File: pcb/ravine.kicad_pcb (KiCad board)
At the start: 2 copper layers, 102 x 101.7 mm, 39 parts

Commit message: okay last save before converting to normie matrix
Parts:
- removed PLACEHOLDER: , placeholder
- added ?: , footprints:xiao-pogo-rev, F.Cu at (155.5, 163.1)
- added CR1: , footprints:bs-2032-8_rev, F.Cu at (185.5, 189.5)
- added D17: , footprints:diode_rev, F.Cu at (198.5, 165.8)
- added D18: , footprints:diode_rev, F.Cu at (204.6, 147.8)
- added D19: , footprints:diode_rev, F.Cu at (210.7, 129.8)
- added D20: , footprints:diode_rev, F.Cu at (220.5, 160.2)
- added D21: , footprints:diode_rev, F.Cu at (226.6, 142.2)
- added D22: , footprints:diode_rev, F.Cu at (231.4, 178.2)
- added D23: , footprints:diode_rev, F.Cu at (160.2, 182.9)
- added D24: , footprints:diode_rev, F.Cu at (160.4, 121.8)
- added D25: , footprints:diode_rev, F.Cu at (156.4, 140.4)
- added D26: , footprints:diode_rev, F.Cu at (175.2, 170.0)
- added XX1: , footprints:slider-mss22d18_rev, F.Cu at (209.0, 186.5)
- B1: footprint E73:SW_TACT_ALPS_SKQGABE010 -> footprints:alps-skqg_rev
- D1, D10, D11, D12, D13, D14, D15, D16, D2, D3, D4, D5, D6, D7, D8, D9: footprint diode-rev -> footprints:diode_rev
- SW1, SW10, SW11, SW12, SW13, SW14, SW15, SW16, SW2, SW3, SW4, SW5, SW6, SW7, SW8, SW9: footprint hs-mx-choc-rev -> footprints:hs-mx-choc_rev
- moved D9 79.9 mm to (157.1, 149.0), turned to 119.333 degrees
- moved D8 71.4 mm to (154.4, 144.1), turned to 119.333 degrees
- moved D7 66.8 mm to (154.3, 148.3), turned to 119.333 degrees
- moved D6 60.5 mm to (151.6, 143.3), turned to 119.333 degrees
- moved D16 58.8 mm to (195.1, 116.5), turned to -18.666 degrees
- moved D3 55.2 mm to (148.7, 146.7), turned to 119.333 degrees
- moved D4 54.7 mm to (148.8, 142.6), turned to 119.333 degrees
- moved D5 52.9 mm to (151.5, 147.5), turned to 119.333 degrees
- moved D2 43.5 mm to (146.0, 141.8), turned to 119.333 degrees
- moved D14 39.9 mm to (183.0, 152.6), turned to -18.6667 degrees
- moved JST1 39.4 mm to (206.0, 194.8), turned to 90 degrees
- moved D1 37.4 mm to (145.9, 145.9), turned to 119.333 degrees
- moved D15 33.2 mm to (189.1, 134.6), turned to -18.6667 degrees
- moved D10 23.4 mm to (157.2, 144.9), turned to 119.333 degrees
- moved D11 10.0 mm to (163.2, 151.7), turned to -15.6667 degrees
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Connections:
- D1 pad 1: middle_bottom -> D6
- D1 pad 2: (no net) -> P6
- D10 pad 1: pinky_top -> D10
- D10 pad 2: P0 -> intr
- D11 pad 2: (no net) -> D9
- D12 pad 2: (no net) -> D9
- D13 pad 2: (no net) -> D9
- D14 pad 1: default_default -> middle_bottom
- D14 pad 2: P3 -> D8
- D15 pad 1: pinky_home -> middle_home
- D15 pad 2: P0 -> D8
- D16 pad 1: default_default -> middle_top
- D16 pad 2: P2 -> D8
- D2 pad 1: middle_home -> D6
- D2 pad 2: (no net) -> intr
- D3 pad 1: middle_top -> D7
- D3 pad 2: (no net) -> P7
- D4 pad 1: index_bottom -> D7
- D4 pad 2: P3 -> intr
- D5 pad 1: index_home -> D8
- D5 pad 2: P3 -> P8
- D6 pad 1: index_top -> D8
- D6 pad 2: P3 -> intr
- D7 pad 1: inner_home -> D9
- D7 pad 2: P4 -> P9
- D8 pad 1: inner_top -> D9
- D8 pad 2: P4 -> intr
- D9 pad 1: default_default -> D10
- D9 pad 2: P0 -> P10
- JST1 pad 1: battery -> jst_bat
- RE1 pad S1: default_default -> P7
- RE1 pad S2: P3 -> default_default
- SW1 pad 1: P1 -> P9
- SW10 pad 1: P1 -> P9
- SW11 pad 1: P0 -> P10
- SW12 pad 1: P1 -> P9
- SW13 pad 1: P0 -> P10
- SW14 pad 1: P3 -> P7
- SW15 pad 1: P3 -> P7
- SW15 pad 2: default_default -> thumb_default
- SW16 pad 1: P4 -> P6
- SW2 pad 1: P0 -> P6
- SW3 pad 1: P2 -> P8
- SW4 pad 1: P4 -> P6
- SW5 pad 1: P0 -> P10
- SW6 pad 1: P4 -> P6
- SW7 pad 1: P1 -> P9
- SW8 pad 1: P0 -> P10
- SW9 pad 1: P2 -> P8
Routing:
- net P10: track 0.00 -> 15.0 mm
- net intr: track 0.00 -> 11.6 mm
- net ring_top: track 0.00 -> 11.1 mm
- net pinky_top: track 0.00 -> 6.15 mm
- net trrs: track 0.00 -> 4.60 mm
- net VCC: track 0.00 -> 4.60 mm
- net D7: track 0.00 -> 4.12 mm
- net D10: track 0.00 -> 4.12 mm
- net D8: track 0.00 -> 4.12 mm
- net D6: track 0.00 -> 4.12 mm
- net D9: track 0.00 -> 4.12 mm
- net middle_top: track 0.00 -> 3.75 mm
- net inner_top: track 0.00 -> 3.75 mm
- net index_top: track 0.00 -> 3.75 mm
- net P6: track 0.00 -> 3.75 mm
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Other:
- board size 102 x 101.7 mm -> 102 x 101.9 mm

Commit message: ok fr this time before matrix
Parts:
- removed the ? at (155.5, 163.1)
- added ?: , xiao-ble, F.Cu at (155.5, 163.1)
- B1: footprint footprints:alps-skqg_rev -> E73:SW_TACT_ALPS_SKQGABE010
- CR1: footprint footprints:bs-2032-8_rev -> bs-2032-8_rev
- D1, D10, D11, D12, D13, D14, D15, D16, D17, D18, D19, D2, D20, D21, D22, D23, D24, D25, D26, D3, D4, D5, D6, D7, D8, D9: footprint footprints:diode_rev -> diode-rev
- SW1, SW10, SW11, SW12, SW13, SW14, SW15, SW16, SW2, SW3, SW4, SW5, SW6, SW7, SW8, SW9: footprint footprints:hs-mx-choc_rev -> hs-mx-choc-rev
- XX1: footprint footprints:slider-mss22d18_rev -> slider-mss22d18_rev
- moved PWR1 0.10 mm to (234.2, 121.9), turned to 45.3333 degrees
- turned D18 to -18.6667 degrees
- turned D15 to -18.6667 degrees
- turned D26 to -18.6667 degrees
- turned TRRS1 to -18.6667 degrees
- turned D4 to 119.333 degrees
- turned SW1 to 169.333 degrees
- turned D24 to 169.333 degrees
- turned D22 to -128.667 degrees
- turned D5 to 119.333 degrees
- turned D8 to 119.333 degrees
- turned D9 to 119.333 degrees
- turned D11 to -15.6667 degrees
- turned SW3 to -15.6667 degrees
- turned SW4 to -15.6667 degrees
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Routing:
- net P10: track 15.0 -> 0.00 mm
- net intr: track 11.6 -> 0.00 mm
- net ring_top: track 11.1 -> 0.00 mm
- net pinky_top: track 6.15 -> 0.00 mm
- net trrs: track 4.60 -> 0.00 mm
- net VCC: track 4.60 -> 0.00 mm
- net D7: track 4.12 -> 0.00 mm
- net D10: track 4.12 -> 0.00 mm
- net D8: track 4.12 -> 0.00 mm
- net D6: track 4.12 -> 0.00 mm
- net D9: track 4.12 -> 0.00 mm
- net middle_top: track 3.75 -> 0.00 mm
- net inner_top: track 3.75 -> 0.00 mm
- net index_top: track 3.75 -> 0.00 mm
- net P6: track 3.75 -> 0.00 mm
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
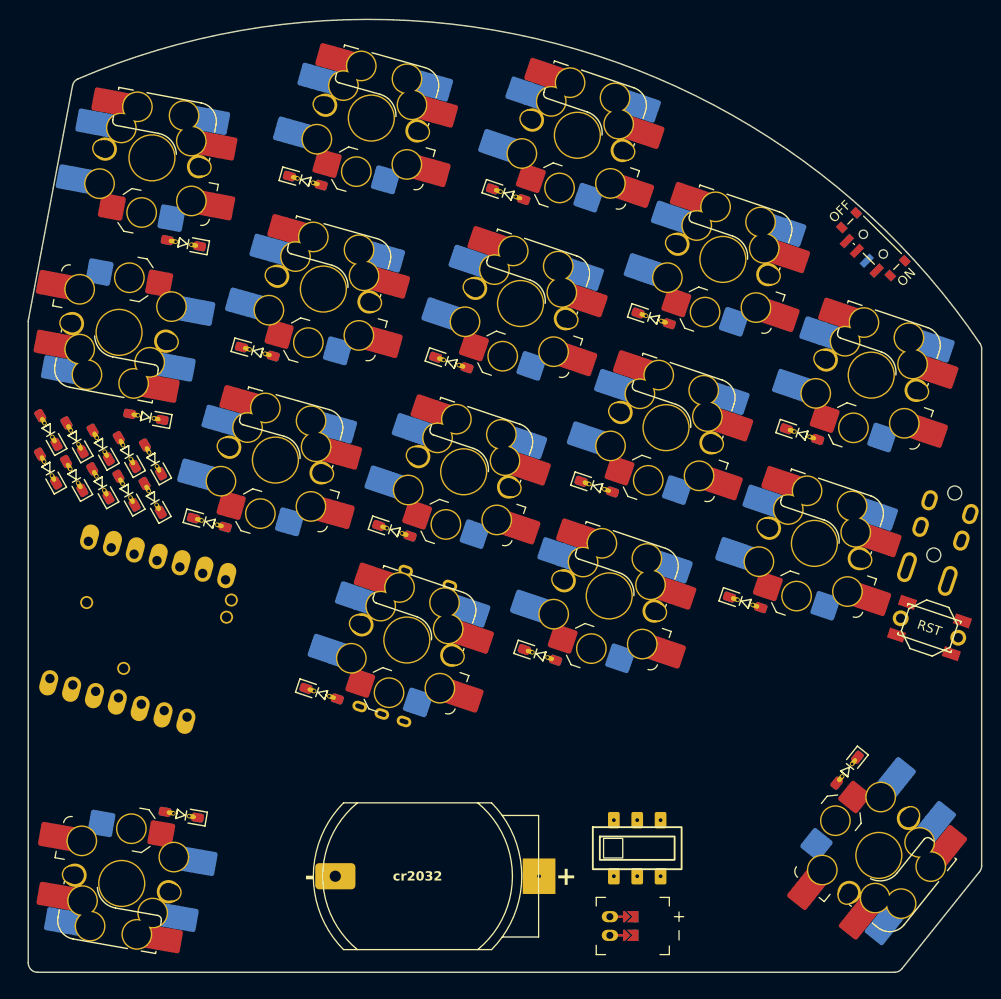
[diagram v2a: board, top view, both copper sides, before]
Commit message: kicadmaxxing, converted to martix
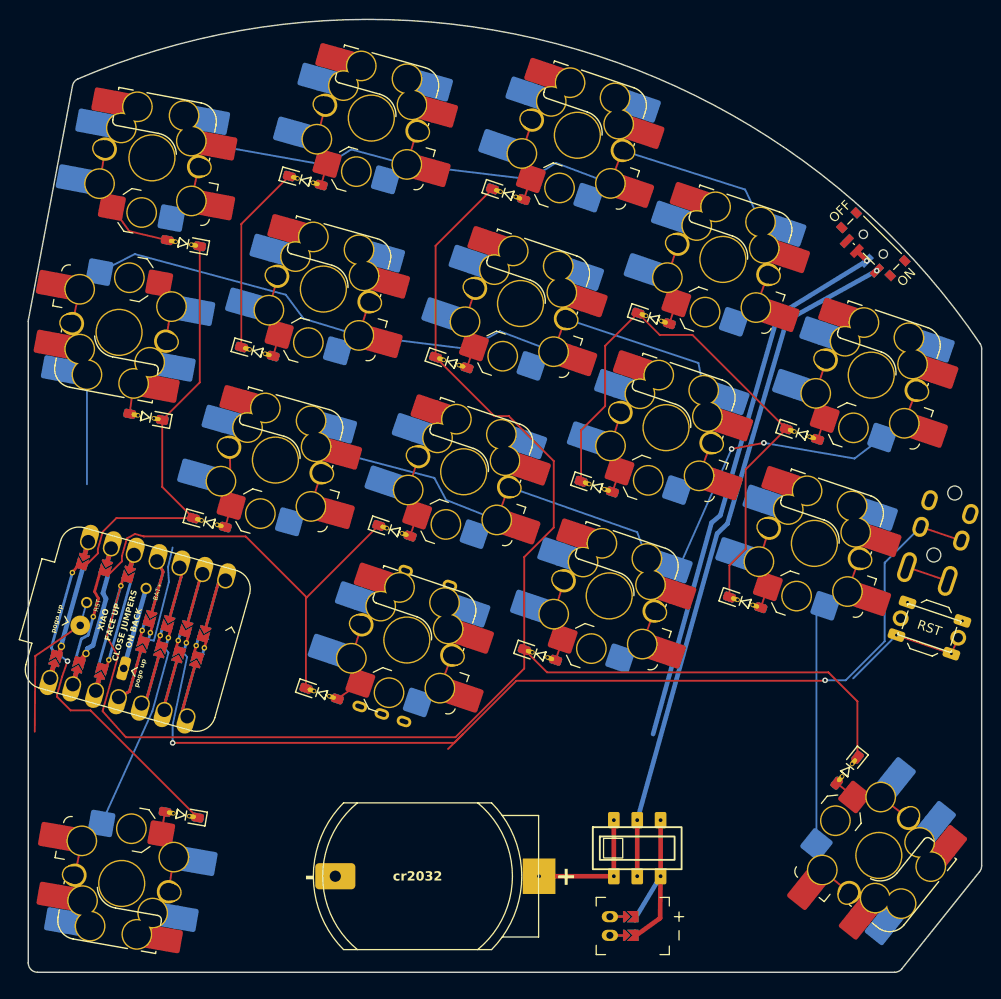
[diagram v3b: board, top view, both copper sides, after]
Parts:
- removed the ? at (155.5, 163.1)
- removed D17, D18, D19, D20, D21, D22, D23, D24, D25, D26: , diode-rev
- added ?: , footprints:xiao-pogo-rev, F.Cu at (155.5, 163.1)
- B1: footprint E73:SW_TACT_ALPS_SKQGABE010 -> footprints:alps-skqg_rev
- D1, D10, D11, D12, D13, D14, D15, D16, D2, D3, D4, D5, D6, D7, D8, D9: footprint diode-rev -> footprints:diode_rev
- moved D12 77.4 mm to (231.4, 178.2), turned to -128.667 degrees
- moved D13 69.1 mm to (160.2, 182.9), turned to 170 degrees
- moved D10 65.2 mm to (220.5, 160.2), turned to -18.6667 degrees
- moved D11 64.1 mm to (226.6, 142.2), turned to -18.6667 degrees
- moved D16 57.0 mm to (175.2, 170.0), turned to -18.6667 degrees
- moved D9 56.9 mm to (210.7, 129.8), turned to -18.6667 degrees
- moved D6 51.2 mm to (195.1, 116.5), turned to -18.6667 degrees
- moved D8 50.4 mm to (204.6, 147.8), turned to -18.6667 degrees
- moved D7 47.6 mm to (198.5, 165.8), turned to -18.6667 degrees
- moved D3 40.1 mm to (173.4, 115.1), turned to -15.6667 degrees
- moved D5 39.7 mm to (189.1, 134.6), turned to -18.6667 degrees
- moved D14 38.2 mm to (160.4, 121.8), turned to 169.333 degrees
- moved D4 35.6 mm to (183.0, 152.6), turned to -18.6667 degrees
- moved D15 33.2 mm to (156.4, 140.4), turned to 169.333 degrees
- moved D2 23.9 mm to (168.3, 133.4), turned to -15.6667 degrees
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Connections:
- D1 pad 1: D6 -> ring_bottom
- D1 pad 2: P6 -> P0
- D10 pad 1: D10 -> inner_home
- D10 pad 2: intr -> P3
- D11 pad 1: ring_bottom -> inner_top
- D11 pad 2: D9 -> P3
- D12 pad 1: ring_home -> thumb_default
- D12 pad 2: D9 -> P2
- D13 pad 1: ring_top -> default_default
- D13 pad 2: D9 -> P0
- D14 pad 1: middle_bottom -> pinky_top
- D14 pad 2: D8 -> P0
- D15 pad 1: middle_home -> pinky_home
- D15 pad 2: D8 -> P0
- D16 pad 1: middle_top -> de
- D16 pad 2: D8 -> P1
- D2 pad 1: D6 -> ring_home
- D2 pad 2: intr -> P1
- D3 pad 1: D7 -> ring_top
- D3 pad 2: P7 -> P1
- D4 pad 1: D7 -> middle_bottom
- D4 pad 2: intr -> P1
- D5 pad 1: D8 -> middle_home
- D5 pad 2: P8 -> P2
- D6 pad 1: D8 -> middle_top
- D6 pad 2: intr -> P2
- D7 pad 1: D9 -> index_bottom
- D7 pad 2: P9 -> P2
- D8 pad 1: D9 -> index_home
- D8 pad 2: intr -> P3
- D9 pad 1: D10 -> index_top
- D9 pad 2: P10 -> P3
- RE1 pad S1: P7 -> de
- RE1 pad S2: default_default -> P4
- SW1 pad 1: P9 -> pinky_home
- SW1 pad 2: pinky_home -> P7
- SW10 pad 1: P9 -> index_home
- SW10 pad 2: index_home -> P7
- SW11 pad 1: P10 -> index_top
- SW11 pad 2: index_top -> P8
- SW12 pad 1: P9 -> inner_home
- SW12 pad 2: inner_home -> P4
- SW13 pad 1: P10 -> inner_top
- SW13 pad 2: inner_top -> P6
- SW14 pad 1: P7 -> de
- SW14 pad 2: default_default -> P4
- SW15 pad 1: P7 -> thumb_default
- SW15 pad 2: thumb_default -> P4
- SW16 pad 1: P6 -> default_default
- SW16 pad 2: default_default -> P4
- SW2 pad 1: P6 -> pinky_top
- SW2 pad 2: pinky_top -> P8
- SW3 pad 1: P8 -> ring_bottom
- SW3 pad 2: ring_bottom -> P6
- SW4 pad 1: P6 -> ring_home
- SW4 pad 2: ring_home -> P7
- SW5 pad 1: P10 -> ring_top
- SW5 pad 2: ring_top -> P8
- SW6 pad 1: P6 -> middle_bottom
- SW6 pad 2: middle_bottom -> P6
- SW7 pad 1: P9 -> middle_home
- SW7 pad 2: middle_home -> P7
- SW8 pad 1: P10 -> middle_top
- SW8 pad 2: middle_top -> P8
- SW9 pad 1: P8 -> index_bottom
- SW9 pad 2: index_bottom -> P6
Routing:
- net P2: track 0.00 -> 168.8 mm
- net trrs: track 0.00 -> 112.0 mm, vias 0 -> 2
- net P7: track 0.00 -> 97.5 mm
- net P6: track 0.00 -> 85.5 mm, vias 0 -> 2
- net P8: track 0.00 -> 79.4 mm
- net P3: track 0.00 -> 73.3 mm
- net battery: track 0.00 -> 73.0 mm, vias 0 -> 1
- net P0: track 0.00 -> 73.0 mm, vias 0 -> 1
- net P1: track 0.00 -> 68.1 mm
- net P4: track 0.00 -> 61.7 mm
- net BAT_POS: track 0.00 -> 59.6 mm, vias 0 -> 1
- net RST: track 0.00 -> 31.1 mm
- net jst_bat: track 0.00 -> 18.7 mm
- net coin_bat: track 0.00 -> 14.0 mm
- net pinky_top: track 0.00 -> 11.1 mm
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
